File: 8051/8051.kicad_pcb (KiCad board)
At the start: 2 copper layers, 70 x 90 mm, 44 parts, among them J1 GND, J10 C_{OUT}, J2 V_{CC}, J3 OUT TX RX V5 G, J4 S + G, J5 G + CK D, J6 AP-B-C, J7 AN-B-C, J8 A_{OUT}, J9 B_{OUT}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

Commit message: almost done(8051)
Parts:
- added C: 0805_p2.0xpad1.0, footprint:0805_p2.0xpad1.0, F.Cu at (92.0, 55.3)
- added REF**: MountingHole_2.1mm, MountingHole:MountingHole_2.1mm, F.Cu at (42.3, 36.9)
- added REF**: MountingHole_2.1mm, MountingHole:MountingHole_2.1mm, F.Cu at (82.7, 115.5)
- added REF**: MountingHole_2.1mm, MountingHole:MountingHole_2.1mm, F.Cu at (91.6, 41.1)
- added REF**: MountingHole_2.1mm, MountingHole:MountingHole_2.1mm, F.Cu at (37.7, 113.0)
- moved R17 97.1 mm to (43.2, 47.0)
- moved R16 92.1 mm to (43.2, 49.6)
- moved C3 66.1 mm to (77.7, 67.1)
- moved J6 46.9 mm to (76.2, 83.3), turned to 0 degrees
- moved REF** 39.5 mm to (40.5, 74.5)
- moved J5 33.4 mm to (66.5, 34.8), turned to 180 degrees
- moved J7 30.5 mm to (62.8, 83.3), turned to 0 degrees
- moved J3 29.6 mm to (35.4, 52.1), turned to 180 degrees
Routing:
- net +3V3: track 131.3 -> 9.95 mm, vias 4 -> 0
- net AOUT: track 0.00 -> 80.5 mm
- net 2D: track 64.7 -> 0.00 mm, vias 2 -> 0
- net CK: track 63.7 -> 0.00 mm, vias 2 -> 0
- net BOUT: track 0.00 -> 63.1 mm, vias 0 -> 2
- net COUT: track 0.00 -> 46.7 mm, vias 0 -> 2
- net CN: track 29.9 -> 47.8 mm, vias 0 -> 1
- net +5V: track 78.2 -> 69.7 mm
- net TXD: track 0.00 -> 6.93 mm
- net RXD: track 0.00 -> 6.93 mm
- net GND: track 50.7 -> 54.6 mm, vias 28 -> 5
- net FC: track 15.8 -> 18.4 mm
- net BN: track 38.7 -> 36.6 mm, vias 0 -> 1
- net AN: track 53.2 -> 51.2 mm
- net BP: track 24.5 -> 22.6 mm, vias 2 -> 1
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
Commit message: 准完成(8051)
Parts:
- moved REF** 12.8 mm to (88.1, 103.9)
- moved REF** 2.83 mm to (34.9, 113.4)
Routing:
- net +5V: track 69.7 -> 139.7 mm
- net TXD: track 6.93 -> 71.6 mm, vias 0 -> 2
- net RXD: track 6.93 -> 70.7 mm, vias 0 -> 2
- net CPOUT: track 0.00 -> 62.2 mm, vias 0 -> 2
- net +3V3: track 9.95 -> 68.2 mm, vias 0 -> 3
- net CK: track 0.00 -> 43.8 mm, vias 0 -> 2
- net 2D: track 0.00 -> 43.6 mm, vias 0 -> 2
- net GND: vias 5 -> 29

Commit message: 打样(8051)日期2022-01-16
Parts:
- moved R1 30.4 mm to (51.6, 67.4), turned to 90 degrees
- moved C4 29.9 mm to (51.6, 62.8), turned to 90 degrees
- moved R2 27.1 mm to (53.7, 62.8), turned to 90 degrees
- moved R5 22.8 mm to (56.9, 62.8), turned to 90 degrees
- moved R4 21.4 mm to (56.9, 67.7), turned to 90 degrees
- moved R12 19.2 mm to (59.2, 63.8), turned to 90 degrees
- moved R7 16.8 mm to (61.6, 62.8), turned to 90 degrees
- moved R6 14.8 mm to (61.6, 67.7), turned to 90 degrees
- moved R11 13.4 mm to (63.8, 63.8), turned to 90 degrees
- moved U3 11.9 mm to (77.8, 62.5), turned to 0 degrees
- moved R9 11.5 mm to (66.3, 62.8), turned to 90 degrees
- moved C1 10.6 mm to (72.7, 61.1), turned to -90 degrees
- moved R10 8.39 mm to (68.4, 63.8), turned to 90 degrees
- moved C3 8.38 mm to (70.5, 62.8), turned to 90 degrees
- moved R8 8.18 mm to (66.3, 67.7), turned to 90 degrees
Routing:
- net AOUT: track 80.5 -> 46.9 mm
- net BOUT: track 63.1 -> 39.1 mm, vias 2 -> 4
- net BN: track 36.6 -> 58.1 mm
- net CN: track 47.8 -> 68.7 mm
- net AN: track 51.2 -> 71.8 mm
- net TXD: track 71.6 -> 52.5 mm
- net BP: track 22.6 -> 39.3 mm
- net CPOUT: track 62.2 -> 45.6 mm, vias 2 -> 0
- net CP: track 14.1 -> 30.0 mm
- net RCP: track 37.7 -> 24.4 mm, vias 2 -> 0
- net RXD: track 70.7 -> 57.6 mm
- net AP: track 37.0 -> 49.7 mm
- net 2D: track 43.6 -> 31.8 mm
- net COUT: track 46.7 -> 35.7 mm, vias 2 -> 4
- net CK: track 43.8 -> 33.7 mm
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
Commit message: digital module
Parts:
- removed C: 0805_p2.0xpad1.0, footprint:0805_p2.0xpad1.0
- removed J1: GND, MountingHole:MountingHole_2.5mm_Pad_TopBottom
- removed J10: C_{OUT}, MountingHole:MountingHole_2.5mm_Pad_TopBottom
- removed J2: V_{CC}, MountingHole:MountingHole_2.5mm_Pad_TopBottom
- removed J7: AN-B-C, footprint:CONN3-P2.54-DR1.0-W1.5
- removed J8: A_{OUT}, MountingHole:MountingHole_2.5mm_Pad_TopBottom
- removed J9: B_{OUT}, MountingHole:MountingHole_2.5mm_Pad_TopBottom
- removed Q1, Q4, Q7: 2N3055, Package_TO_SOT_SMD:SOT-23
- removed Q2, Q5, Q8: nfet, footprint:SOIC-8
- removed Q3, Q6, Q9: pfet, footprint:SOIC-8
- removed R15, R16, R17: 1K, footprint:0603_p1.7xpad1.0
- removed REF** (x4): MountingHole_2.1mm, MountingHole:MountingHole_2.1mm
- removed REF**: KiCad-Logo_5mm_SilkScreen, Symbol:KiCad-Logo_5mm_SilkScreen
- added C5: C, footprint:0805_p2.0xpad1.0, F.Cu at (86.7, 28.8)
- added C6: C, footprint:0805_p2.0xpad1.0, F.Cu at (86.7, 43.8)
- added C7: C, footprint:0805_p2.0xpad1.0, F.Cu at (86.7, 58.8)
- added D1: D, footprint:0805_p2.0xpad1.0, F.Cu at (80.2, 25.7)
- added D2: D, footprint:0805_p2.0xpad1.0, F.Cu at (80.2, 40.7)
- added D3: D, footprint:0805_p2.0xpad1.0, F.Cu at (80.2, 55.7)
- added U4: IR2103, footprint:SOIC-8, F.Cu at (79.7, 30.4)
- added U5: IR2103, footprint:SOIC-8, F.Cu at (79.7, 45.4)
- added U6: IR2103, footprint:SOIC-8, F.Cu at (79.7, 60.4)
- J3: value OUT TX RX V5 G -> S + G; footprint Connector_PinHeader_2.54mm:PinHeader_1x05_P2.54mm_Vertical -> Connector_PinHeader_2.54mm:PinHeader_1x03_P2.54mm_Vertical
- J4: value S + G -> OUT TX RX V5 G; footprint Connector_PinHeader_2.54mm:PinHeader_1x03_P2.54mm_Vertical -> Connector_PinHeader_2.54mm:PinHeader_1x05_P2.54mm_Vertical
- J6: value AP-B-C -> Conn_01x11; footprint footprint:CONN3-P2.54-DR1.0-W1.5 -> Connector_PinHeader_2.54mm:PinHeader_1x11_P2.54mm_Vertical
- R11: value 47K -> 10K
- R13, R14: value 1K -> 47K
- R3, R4: value 47K -> 1K
- R5: value 10K -> 47K
- moved U1 67.9 mm to (36.5, 34.0), turned to 0 degrees
- moved C2 60.9 mm to (34.7, 39.7), turned to 0 degrees
- moved U2 59.5 mm to (34.7, 45.1), turned to 180 degrees
- moved J6 55.5 mm to (96.6, 31.7)
- moved J4 52.9 mm to (41.0, 65.6)
- moved R5 48.0 mm to (25.1, 26.8), turned to 0 degrees
- moved R14 45.9 mm to (57.4, 47.9), turned to 180 degrees
- moved R13 41.9 mm to (57.4, 52.8), turned to 180 degrees
- moved R3 40.0 mm to (47.3, 58.4), turned to 0 degrees
- moved U3 35.7 mm to (56.2, 34.0), turned to 90 degrees
- moved C3 33.9 mm to (41.5, 45.2), turned to -90 degrees
- moved C1 29.0 mm to (54.8, 38.3), turned to 0 degrees
- moved R10 24.3 mm to (60.6, 40.8), turned to 180 degrees
- moved R11 24.2 mm to (56.5, 40.8), turned to 180 degrees
- moved J3 23.5 mm to (23.4, 32.0), turned to 0 degrees
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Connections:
- J3 pad 1: CPOUT -> Net-(J3-Pad1)
- J3 pad 2: TXD -> +5V
- J3 pad 3: RXD -> GND
- J4 pad 1: Net-(J4-Pad1) -> CPOUT
- J4 pad 2: +5V -> TXD
- J4 pad 3: GND -> RXD
- J6 pad 1: AP -> VCC
- J6 pad 2: BP -> DAP
- J6 pad 3: CP -> AOUT
- R10 pad 1: FC -> COUT
- R10 pad 2: F_ABC -> FC
- R11 pad 1: FB -> FC
- R11 pad 2: F_ABC -> GND
- R12 pad 1: FA -> FC
- R13 pad 1: VCC -> FB
- R13 pad 2: Net-(Q1-Pad3) -> F_ABC
- R14 pad 1: VCC -> FA
- R14 pad 2: Net-(Q4-Pad3) -> F_ABC
- R3 pad 1: Net-(J4-Pad1) -> TXD
- R3 pad 2: RCP -> +5V
- R4 pad 1: AOUT -> RXD
- R4 pad 2: FA -> +5V
- R5 pad 1: FA -> Net-(J3-Pad1)
- R5 pad 2: GND -> RCP
- R6 pad 1: BOUT -> AOUT
- R6 pad 2: FB -> FA
- R7 pad 1: FB -> FA
- R8 pad 1: COUT -> BOUT
- R8 pad 2: FC -> FB
- R9 pad 1: FC -> FB
- U3 pad 10: AP -> CP
- U3 pad 13: CP -> AP
- U3 pad 19: RCP -> CPOUT
- U3 pad 20: CPOUT -> RCP
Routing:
- net +5V: track 139.7 -> 21.9 mm, vias 1 -> 0
- net RXD: track 57.6 -> 0.00 mm, vias 2 -> 0
- net TXD: track 52.5 -> 0.00 mm, vias 2 -> 0
- net AN: track 71.8 -> 24.7 mm, vias 0 -> 2
- net CPOUT: track 45.6 -> 0.00 mm
- net +3V3: track 69.5 -> 24.5 mm, vias 3 -> 2
- net VCC: track 179.1 -> 140.5 mm
- net CK: track 33.7 -> 0.00 mm, vias 2 -> 0
- net 2D: track 31.8 -> 0.00 mm, vias 2 -> 0
- net AP: track 49.7 -> 22.7 mm, vias 1 -> 2
- net GND: track 54.6 -> 28.1 mm, vias 29 -> 0
- net RCP: track 24.4 -> 0.00 mm
- net COUT: track 35.7 -> 57.8 mm, vias 4 -> 2
- net Net-(Q4-Pad3): track 20.4 -> 0.00 mm
- net Net-(Q1-Pad3): track 20.0 -> 0.00 mm
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- removed copper zone on F.Cu, net AOUT
- removed copper zone on F.Cu, net BOUT
- removed copper zone on F.Cu, net COUT
- removed copper zone on F.Cu, net GND
- removed copper zone on F.Cu, net VCC
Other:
- board size 70 x 90 mm -> 80 x 50 mm
- board text added: "保護傘"

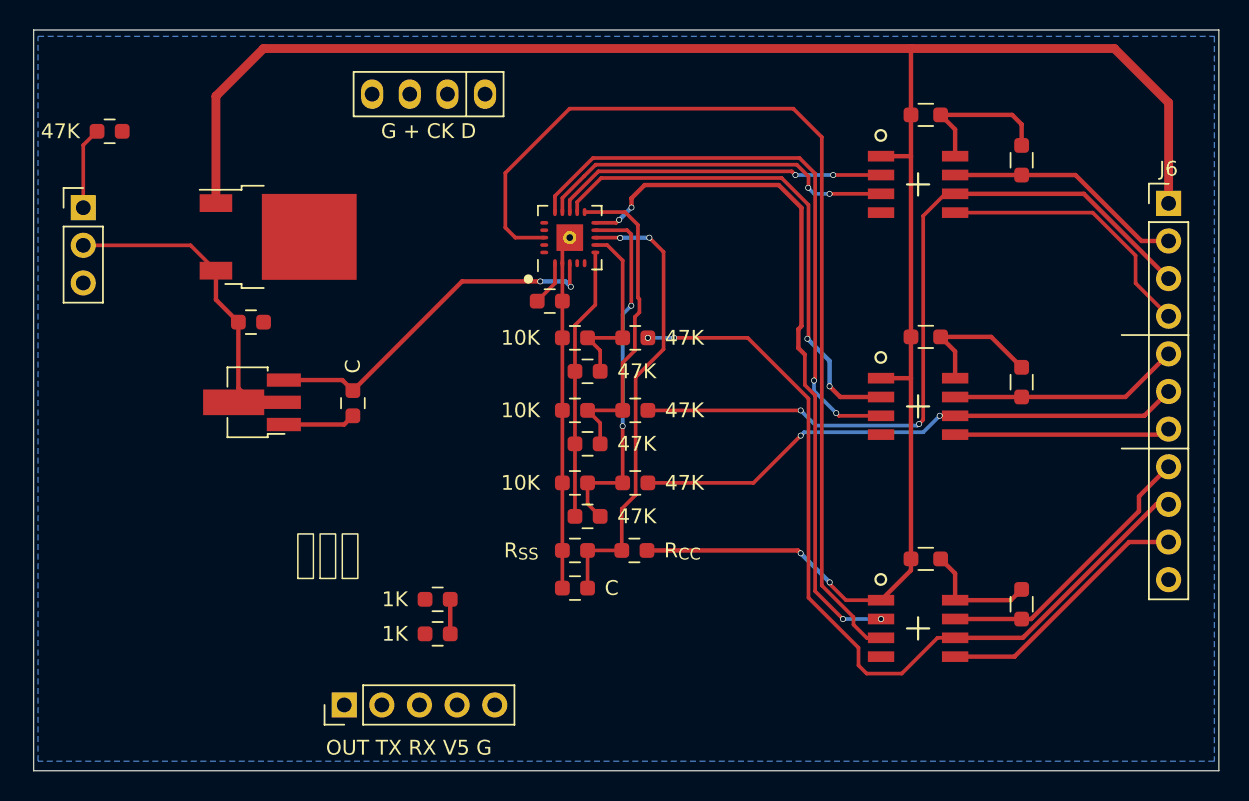
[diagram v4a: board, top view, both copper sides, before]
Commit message: 已经打样，但是3伏和5伏的稳压没有做到地的过孔
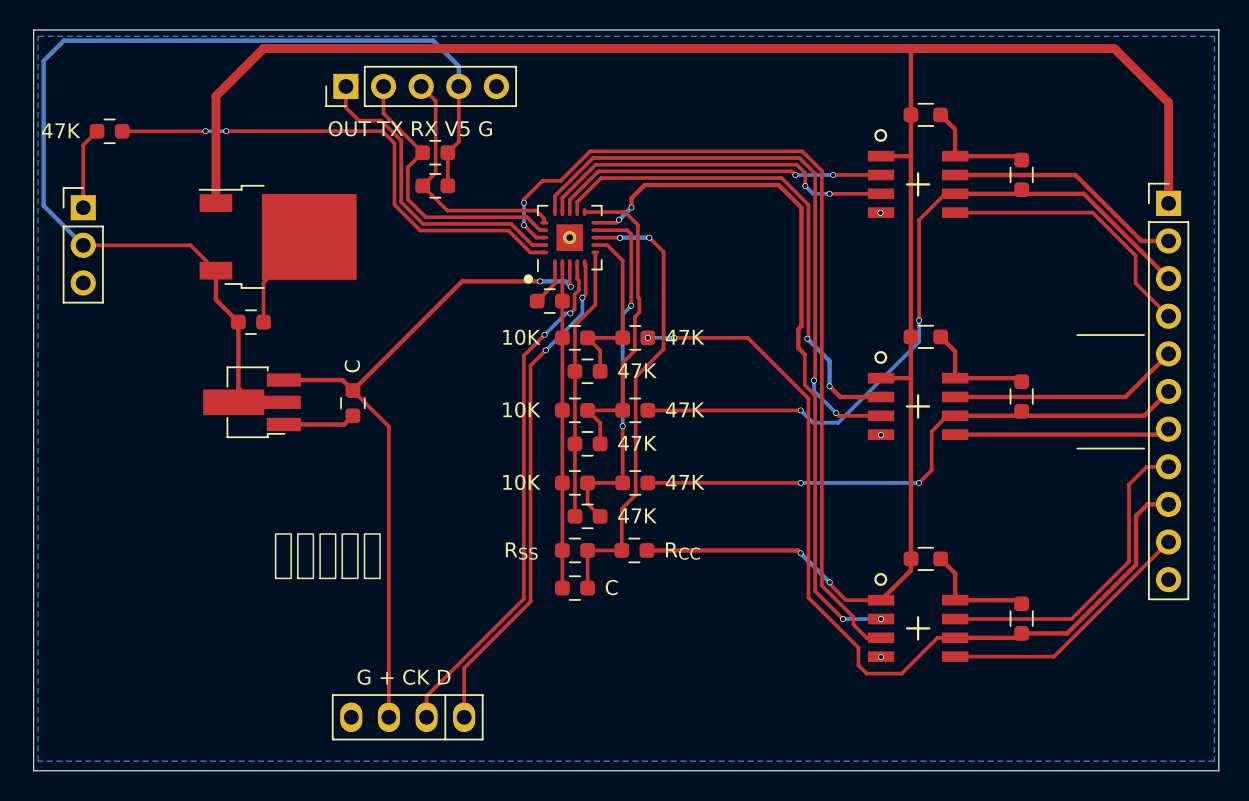
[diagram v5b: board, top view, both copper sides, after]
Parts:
- moved J5 42.1 mm to (45.2, 66.4)
- moved J4 41.8 mm to (41.1, 23.8)
- moved R4 30.2 mm to (47.1, 30.5)
- moved R3 30.2 mm to (47.1, 28.3)
- moved C5 0.99 mm to (86.7, 29.8)
- moved C6 0.97 mm to (86.7, 44.7)
- moved C7 0.97 mm to (86.7, 59.7)
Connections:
- C5 pad 2: DAP -> AOUT
- C6 pad 2: DBP -> BOUT
- C7 pad 2: DCP -> COUT
- U3 pad 21: GND -> (no net)
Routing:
- net +5V: track 21.9 -> 70.8 mm
- net CK: track 0.00 -> 35.1 mm, vias 0 -> 2
- net RCP: track 0.00 -> 34.3 mm, vias 0 -> 2
- net 2D: track 0.00 -> 34.1 mm, vias 0 -> 2
- net +3V3: track 24.5 -> 47.5 mm
- net CPOUT: track 0.00 -> 21.1 mm
- net TXD: track 0.00 -> 19.2 mm
- net RXD: track 0.00 -> 16.9 mm
- net CN: track 66.6 -> 59.2 mm, vias 0 -> 2
- net GND: track 28.1 -> 33.9 mm, vias 0 -> 3
- net AOUT: track 51.8 -> 48.4 mm
- net Net-(C5-Pad1): track 10.3 -> 7.42 mm
- net DCP: track 19.3 -> 21.7 mm
- net Net-(C6-Pad1): track 9.51 -> 7.45 mm
- net COUT: track 57.8 -> 59.3 mm
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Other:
- board text added: "床前明月光"
- board text removed: "保護傘"
